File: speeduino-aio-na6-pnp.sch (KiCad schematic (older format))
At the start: 10 parts

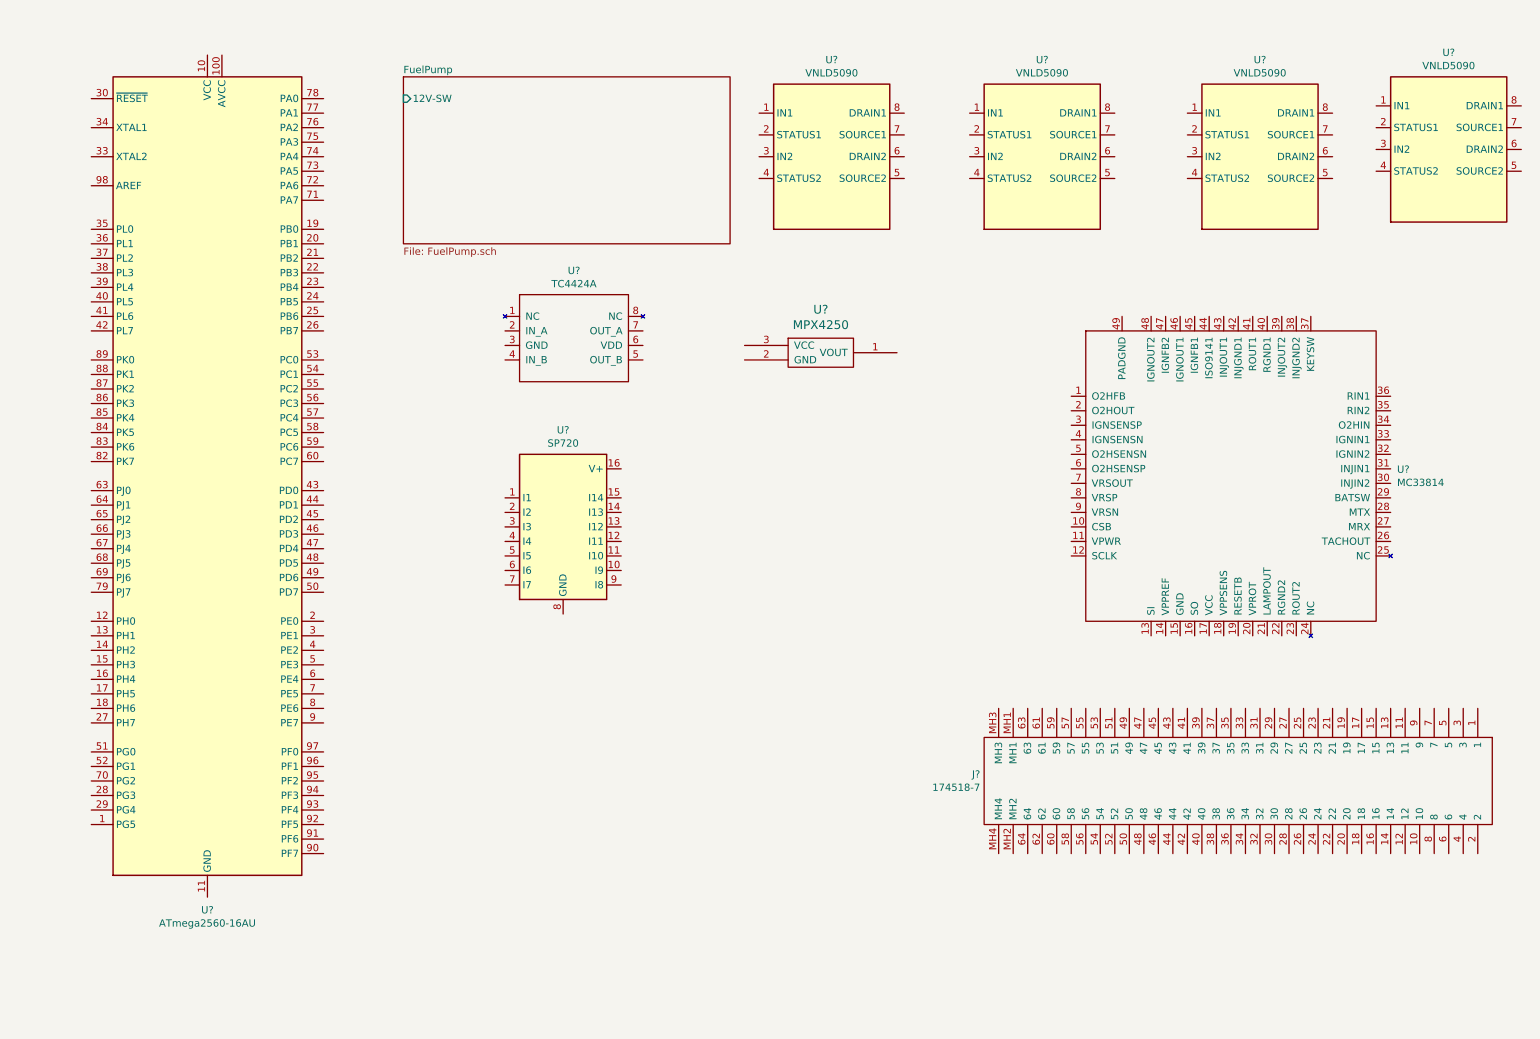
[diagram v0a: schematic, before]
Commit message: Almost finished w/ schematic
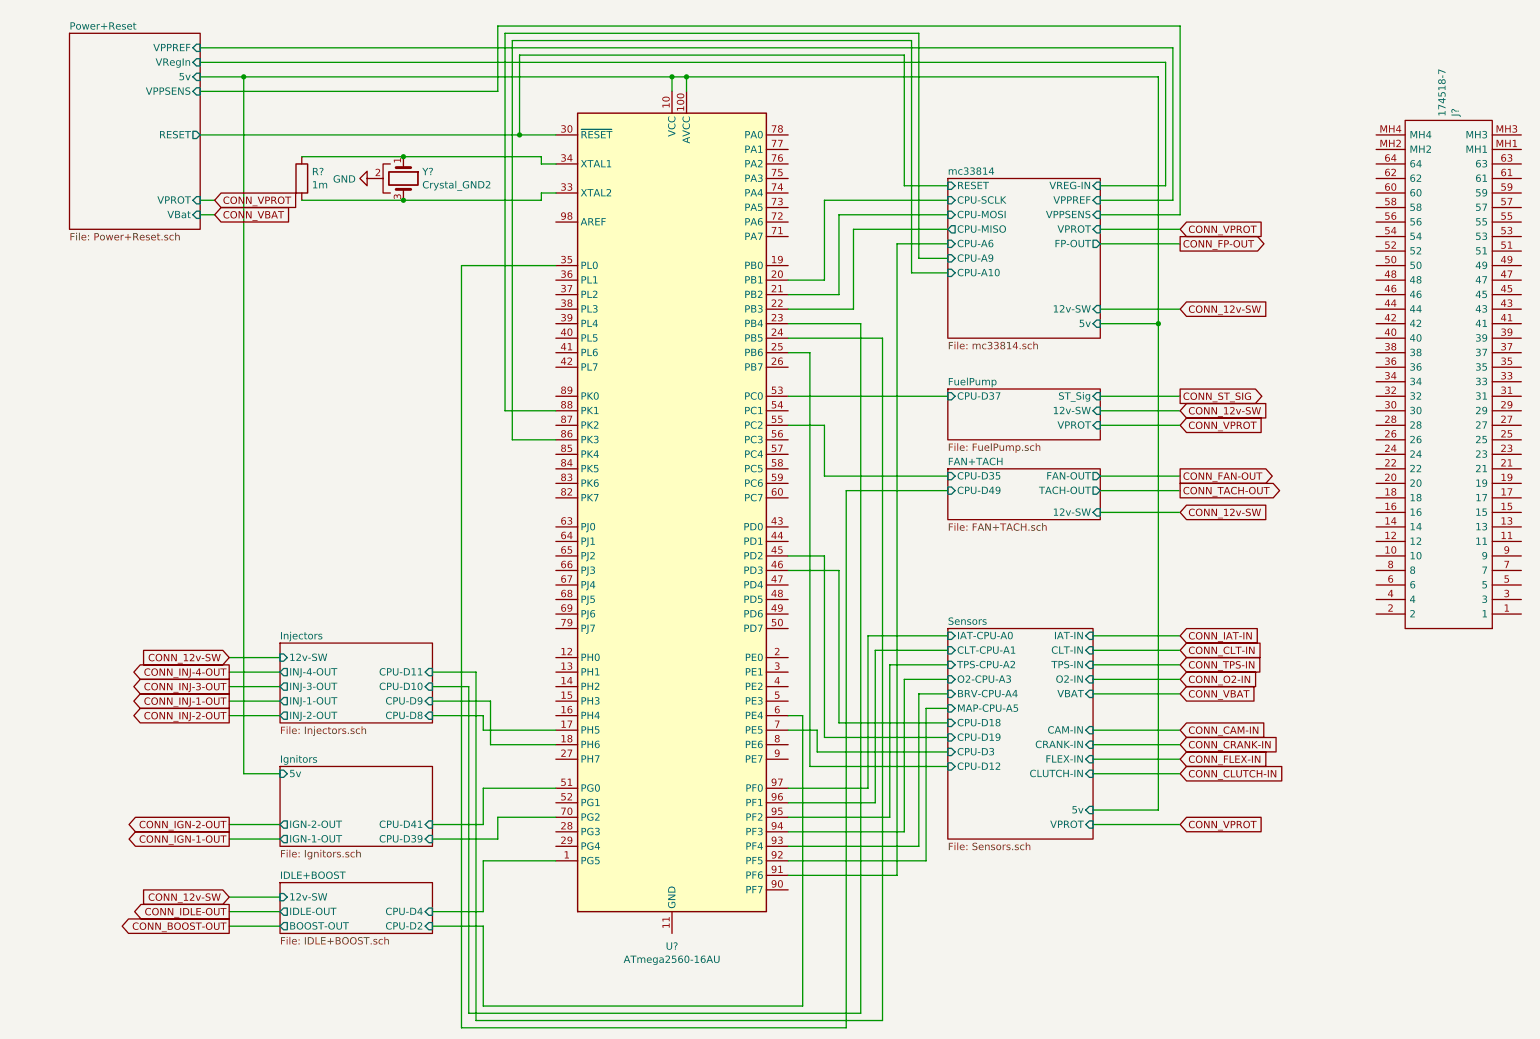
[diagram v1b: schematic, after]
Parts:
- removed U?: TC4424A, Package_SO:SOIC-8_3.9x4.9mm_P1.27mm, symbol speeduino_ic_automotive:TC4424A
- removed U?: SP720, Package_SO:SOIC-16_3.9x9.9mm_P1.27mm, symbol speeduino_ic_automotive:SP720
- removed U?: MPX4250, symbol speeduino_misc:MPX4250
- removed U? (x4): VNLD5090, Package_SO:SO-8_3.9x4.9mm_P1.27mm, symbol speeduino_ic_automotive:VNLD5090
- removed U?: MC33814, Package_QFP:LQFP-48-1EP_7x7mm_P0.5mm_EP3.6x3.6mm_ThermalVias, symbol speeduino_ic_automotive:MC33814
- added R?: 1m, Resistor_SMD:R_0603_1608Metric_Pad1.05x0.95mm_HandSolder, symbol Device:R
- added Y?: Crystal_GND2, Crystal:Crystal_SMD_3225-4Pin_3.2x2.5mm_HandSoldering, symbol Device:Crystal_GND2
- U?: LCSC_FP (none) -> TQFP-100_14.0x14.0x0.5P; LCSC_PN (none) -> C22460
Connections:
- net IDLE+BOOST/CPU-D4: now reaches U?.1 (PG5)
- net Ignitors/5v: now reaches U?.10 (VCC), U?.31 (VCC), U?.61 (VCC), U?.80 (VCC)
- net Ignitors/5v: now also U?.100 (AVCC)
- net Injectors/CPU-D8: now reaches U?.17 (PH5)
- net Injectors/CPU-D9: now reaches U?.18 (PH6)
- net mc33814/CPU-SCLK: now reaches U?.20 (PB1)
- net mc33814/CPU-MOSI: now reaches U?.21 (PB2)
- net mc33814/CPU-MISO: now reaches U?.22 (PB3)
- net Injectors/CPU-D10: now reaches U?.23 (PB4)
- net Injectors/CPU-D11: now reaches U?.24 (PB5)
- net Sensors/CPU-D12: now reaches U?.25 (PB6)
- net Power+Reset/RESET: now reaches U?.30 (~RESET)
- net at U?.33 (XTAL2): now also R?.2, Y?.3
- net at U?.34 (XTAL1): now also R?.1, Y?.1
- net FAN+TACH/CPU-D49: now reaches U?.35 (PL0)
- net Sensors/CPU-D19: now reaches U?.45 (PD2)
- net Sensors/CPU-D18: now reaches U?.46 (PD3)
- net Ignitors/CPU-D41: now reaches U?.51 (PG0)
- net FuelPump/CPU-D37: now reaches U?.53 (PC0)
- net FAN+TACH/CPU-D35: now reaches U?.55 (PC2)
- net IDLE+BOOST/CPU-D2: now reaches U?.6 (PE4)
- net Sensors/CPU-D3: now reaches U?.7 (PE5)
- net Ignitors/CPU-D39: now reaches U?.70 (PG2)
- net mc33814/CPU-A10: now reaches U?.86 (PK3)
- net mc33814/CPU-A9: now reaches U?.88 (PK1)
- net mc33814/CPU-A6: now reaches U?.91 (PF6)
- net Sensors/MAP-CPU-A5: now reaches U?.92 (PF5)
- net Sensors/BRV-CPU-A4: now reaches U?.93 (PF4)
- net Sensors/O2-CPU-A3: now reaches U?.94 (PF3)
- net Sensors/TPS-CPU-A2: now reaches U?.95 (PF2)
- net Sensors/CLT-CPU-A1: now reaches U?.96 (PF1)
- net Sensors/IAT-CPU-A0: now reaches U?.97 (PF0)
- new net GND: Y?.2
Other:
- moved on the sheet: J?, U?

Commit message: Starting on layout
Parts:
- removed J?: 174518-7, 1745187, symbol speeduino_connector_automotive:174518-7
- added J1: Conn_02x03_Odd_Even, Connector_PinHeader_2.54mm:PinHeader_2x03_P2.54mm_Vertical_SMD, symbol Connector_Generic:Conn_02x03_Odd_Even
- added J2: Conn_01x06, Connector_PinHeader_2.54mm:PinHeader_1x06_P2.54mm_Vertical_SMD_Pin1Left, symbol Connector_Generic:Conn_01x06
- gave numbers to parts that had none: 3
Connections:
- net GND: now also J1.6 (Pin_6), J2.6 (Pin_6)
- net Power+Reset/RESET: now also J1.5 (Pin_5), J2.1 (Pin_1)
- net mc33814/CPU-MISO: now also J1.1 (Pin_1)
- net mc33814/CPU-MOSI: now also J1.4 (Pin_4)
- net mc33814/CPU-SCLK: now also J1.3 (Pin_3)
- net at U1.2 (PE0): now also J2.3 (Pin_3)
- net at U1.3 (PE1): now also J2.2 (Pin_2)
- net Ignitors/CPU-D32: now reaches U1.57 (PC4)
- net Ignitors/CPU-D33: now reaches U1.58 (PC5)
- net Ignitors/5v renamed CONN_5v
- net CONN_5v: now also J1.2 (Pin_2), J2.4 (Pin_4)
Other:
- note added: "FTDI"
- note added: "ICSP"
- moved on the sheet: R1, U1, Y1

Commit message: restart a third time
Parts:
- removed J1: Conn_02x03_Odd_Even, Connector_PinHeader_2.54mm:PinHeader_2x03_P2.54mm_Vertical_SMD, symbol Connector_Generic:Conn_02x03_Odd_Even
- removed J2: Conn_01x06, Connector_PinHeader_2.54mm:PinHeader_1x06_P2.54mm_Vertical_SMD_Pin1Left, symbol Connector_Generic:Conn_01x06
- removed R1: 1m, Resistor_SMD:R_0603_1608Metric_Pad1.05x0.95mm_HandSolder, symbol Device:R
- removed U1: ATmega2560-16AU, Package_QFP:TQFP-100_14x14mm_P0.5mm, symbol MCU_Microchip_ATmega:ATmega2560-16AU
- removed Y1: Crystal_GND2, Crystal:Crystal_SMD_3225-4Pin_3.2x2.5mm_HandSoldering, symbol Device:Crystal_GND2
- added H1, H2, H3, H4: MountingHole_Pad, MountingHole:MountingHole_4.3mm_M4_Pad_Via, symbol Mechanical:MountingHole_Pad
- added J1: CONN_BLACK, speeduino_connector_automotive:Delphi_Sicma_24_Black, symbol speeduino_connector_automotive:Delphi_Sicma_24
- added J2: CONN_GREY, speeduino_connector_automotive:Delphi_Sicma_24_Grey, symbol speeduino_connector_automotive:Delphi_Sicma_24
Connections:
- net GND: now also H1.1, H2.1, H3.1, H4.1, J1.B1, J1.B2, J1.B3, J1.B4, J1.B5, J1.B6, J1.B7, J2.B3, J2.B4, J2.B5, J2.B6, J2.B7, J2.B8, J2.C5, J2.C6, J2.C7
- new net 12v-SW: J1.A2
- new net BOOST: J2.C4
- new net CAM: J2.A2
- new net CANH: J2.B1
- new net CANL: J2.B2
- new net CLT: J2.A6
- new net CLUTCH: J2.A3
- new net CRANK: J2.A1
- new net FAN: J2.C1
- new net FLEX: J2.C8
- new net FP: J2.A8
- new net IAT: J2.A7
- new net IDLE: J2.C3
- new net IGN-1: J1.C5
- new net IGN-2: J1.C6
- new net IGN-3: J1.C7
- new net IGN-4: J1.C8
- new net INJ-1: J1.C1
- new net INJ-2: J1.C2
- new net INJ-3: J1.C3
- new net INJ-4: J1.C4
- new net O2: J2.A4
- new net ST_SIG: J1.B8
- new net TACH: J2.C2
- new net TPS: J2.A5
- new net VBAT: J1.A1
- new net VPROT: J1.A8
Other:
- note removed: "FTDI"
- note removed: "ICSP"

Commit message: Layout p much finished.. Time for some stretch goals..?
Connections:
- net FAN: now also J2.C2; no longer J2.C1
- net FP: now also J2.B3; no longer J2.A8
- net GND: now also J1.B8; no longer J1.B1, J2.B3
- net IGN-1: now also J1.C2; no longer J1.C5
- net IGN-2: now also J1.C1; no longer J1.C6
- net IGN-3: now also J1.C4; no longer J1.C7
- net IGN-4: now also J1.C3; no longer J1.C8
- net INJ-1: now also J1.C6; no longer J1.C1
- net INJ-2: now also J1.C5; no longer J1.C2
- net INJ-3: now also J1.C8; no longer J1.C3
- net INJ-4: now also J1.C7; no longer J1.C4
- net ST_SIG: now also J1.B1; no longer J1.B8
- net TACH: now also J2.C1; no longer J2.C2
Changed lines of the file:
@@
 Text GLabel 7650 2150 0    50   Input ~ 0
 12v-SW
-Text GLabel 9000 2250 2    50   Output ~ 0
+Text GLabel 9000 1750 2    50   Output ~ 0
 INJ-1
-Text GLabel 9000 2150 2    50   Output ~ 0
+Text GLabel 9000 1850 2    50   Output ~ 0
 INJ-2
-Text GLabel 9000 2050 2    50   Output ~ 0
+Text GLabel 9000 1550 2    50   Output ~ 0
 INJ-3
-Text GLabel 9000 1950 2    50   Output ~ 0
+Text GLabel 9000 1650 2    50   Output ~ 0
 INJ-4
 Text GLabel 5200 1750 2    50   Output ~ 0
@@
 Wire Wire Line
 	7650 2250 7800 2250
-Text GLabel 9000 1550 2    50   Output ~ 0
+Text GLabel 9000 2050 2    50   Output ~ 0
 IGN-4
-Text GLabel 9000 1650 2    50   Output ~ 0
+Text GLabel 9000 1950 2    50   Output ~ 0
 IGN-3
-Text GLabel 9000 1750 2    50   Output ~ 0
-IGN-2
-Text GLabel 9000 1850 2    50   Output ~ 0
-IGN-1
 Wire Wire Line
 	9000 1850 8700 1850
+Text GLabel 9000 3600 2    50   Output ~ 0
+FAN
 Text GLabel 9000 3700 2    50   Output ~ 0
-FAN
-Text GLabel 9000 3600 2    50   Output ~ 0
 TACH
 Text GLabel 9000 3500 2    50   Output ~ 0
@@
 Text GLabel 5200 3550 2    50   Output ~ 0
 FP
-Text GLabel 7650 3000 0    50   Output ~ 0
+Text GLabel 8200 3900 3    50   Output ~ 0
 FP
-Wire Wire Line
-	7650 3000 8150 3000
 Text GLabel 7650 2250 0    50   Input ~ 0
 VBAT
@@
 Wire Wire Line
 	7650 1550 8150 1550
-Text GLabel 8700 2450 3    50   Input ~ 0
+Text GLabel 8000 2450 3    50   Input ~ 0
 ST_SIG
 Text GLabel 5250 6100 2    50   Input ~ 0
@@
 L power:GND #PWR0101
 U 1 1 609457BA
-P 8000 2550
-F 0 "#PWR0101" H 8000 2300 50  0001 C CNN
-F 1 "GND" H 8005 2377 50  0000 C CNN
-F 2 "" H 8000 2550 50  0001 C CNN
-F 3 "" H 8000 2550 50  0001 C CNN
-	1    8000 2550
-	1    0    0    -1
-$EndComp
-Wire Wire Line
-	8000 2450 8000 2500
-Wire Wire Line
-	8000 2500 8100 2500
+P 8700 2600
+F 0 "#PWR0101" H 8700 2350 50  0001 C CNN
+F 1 "GND" H 8705 2427 50  0000 C CNN
+F 2 "" H 8700 2600 50  0001 C CNN
+F 3 "" H 8700 2600 50  0001 C CNN
+	1    8700 2600
+	1    0    0    -1
+$EndComp
 Wire Wire Line
 	8100 2500 8100 2450
-Connection ~ 8000 2500
-Wire Wire Line
-	8000 2500 8000 2550
 Wire Wire Line
 	8100 2500 8200 2500
 Wire Wire Line
 	8600 2500 8600 2450
-Connection ~ 8100 2500
 Wire Wire Line
 	8500 2450 8500 2500
@@
 Wire Wire Line
 	8700 3900 8700 3950
-Wire Wire Line
-	8200 3900 8200 3950
-Wire Wire Line
-	8200 3950 8300 3950
 Connection ~ 8700 3950
 Wire Wire Line
@@
 Wire Wire Line
 	8300 3900 8300 3950
-Connection ~ 8300 3950
 Wire Wire Line
 	8300 3950 8400 3950
@@
 	9000 3300 9000 3200
 Connection ~ 9000 3200
+Text GLabel 9000 2150 2    50   Output ~ 0
+IGN-1
+Text GLabel 9000 2250 2    50   Output ~ 0
+IGN-2
+Wire Wire Line
+	8600 2500 8700 2500
+Wire Wire Line
+	8700 2500 8700 2450
+Connection ~ 8600 2500
+Wire Wire Line
+	8700 2600 8700 2500
+Connection ~ 8700 2500
 $EndSCHEMATC
